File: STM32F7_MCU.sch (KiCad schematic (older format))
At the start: 49 parts, among them IC4 STM32F769IIT6, IC5 LD1117ADT33TR, Y1 25MHz, Y2 XTAL016178-85SMX

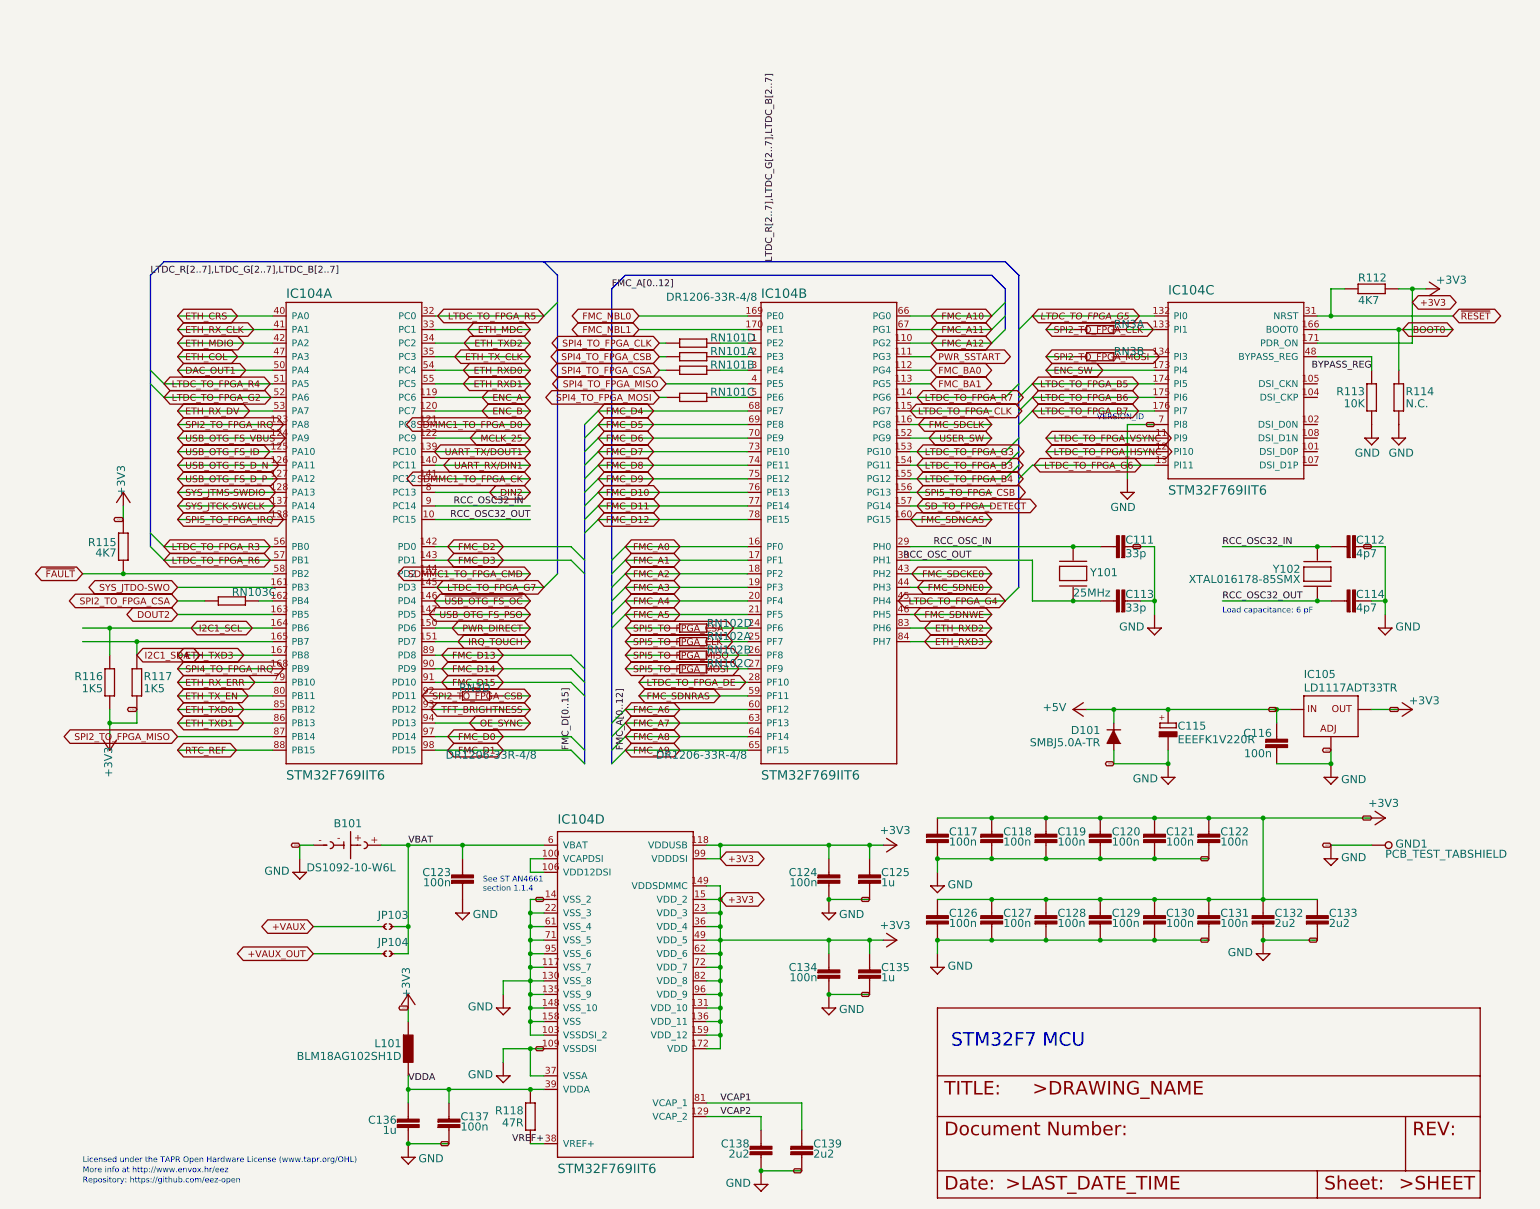
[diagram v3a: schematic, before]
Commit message: Removing BUS from STM32 - cleanup direct connections
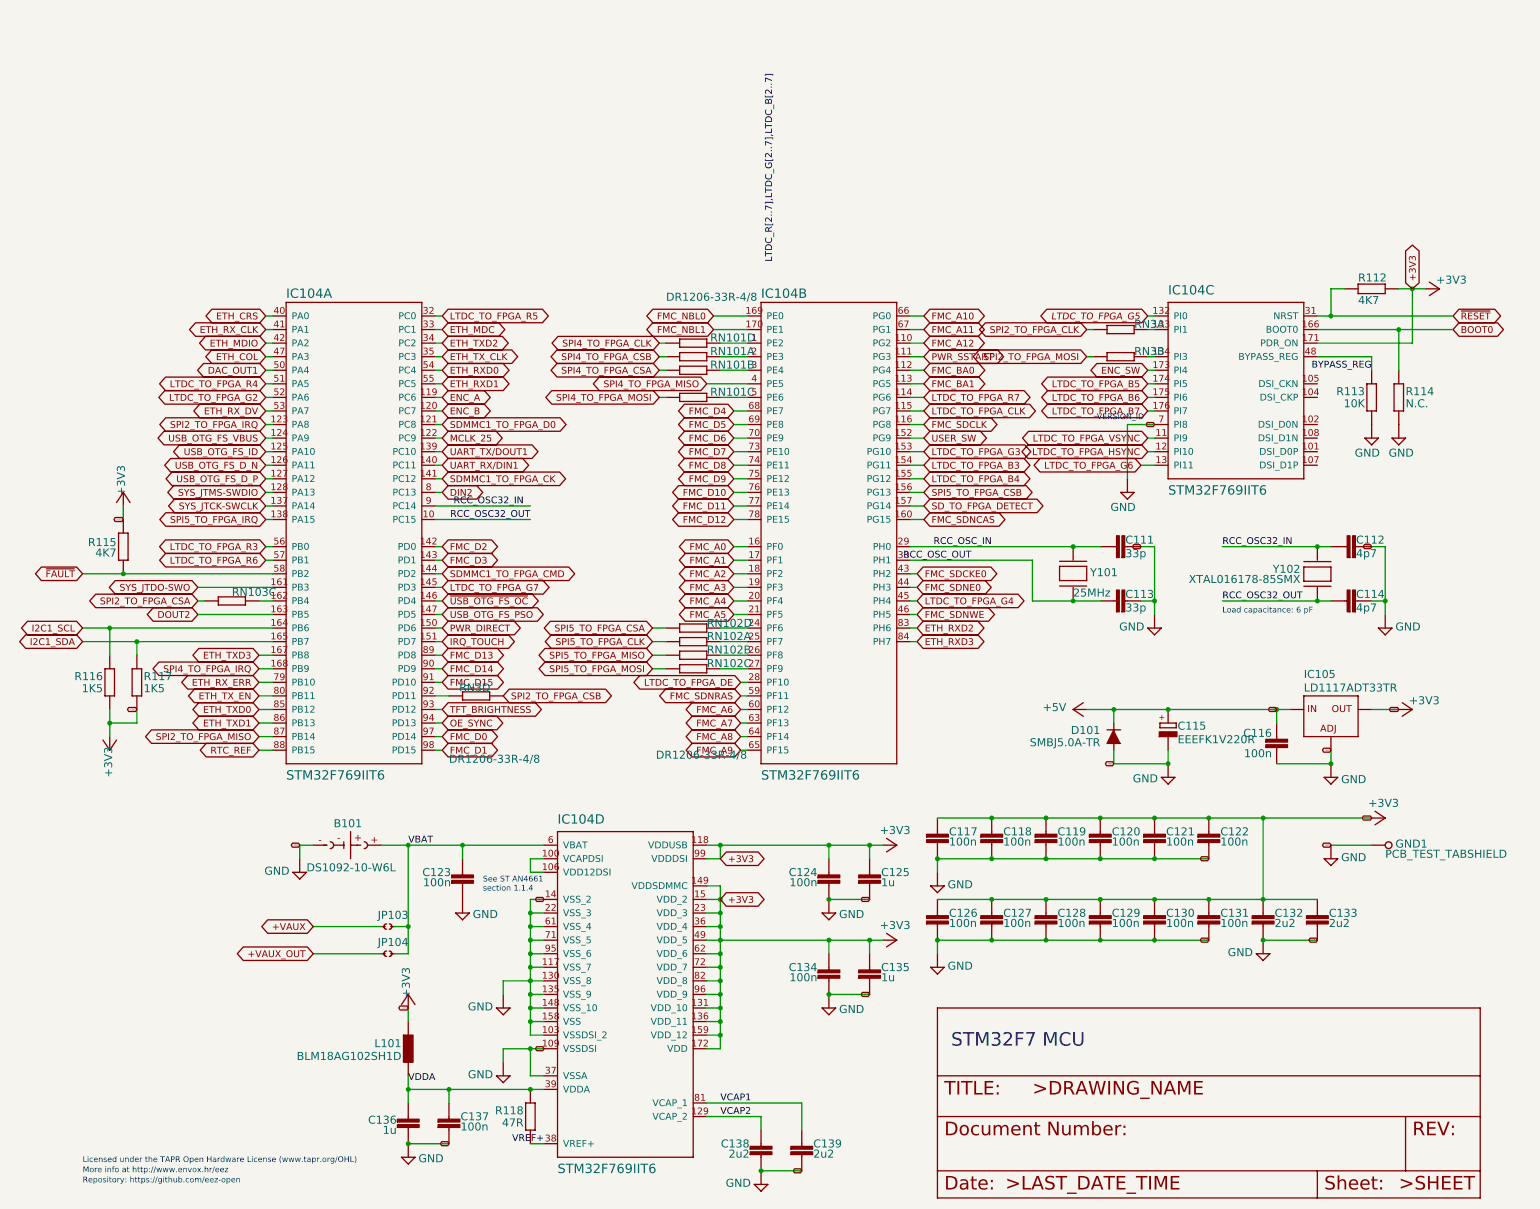
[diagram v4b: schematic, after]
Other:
- moved on the sheet: RN3A, RN3B

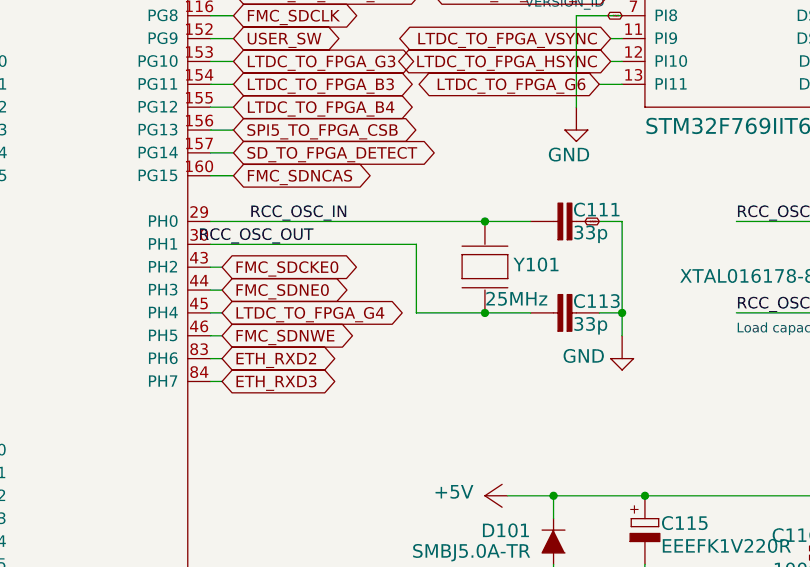
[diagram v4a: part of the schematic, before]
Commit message: Adding SPI from FPGA
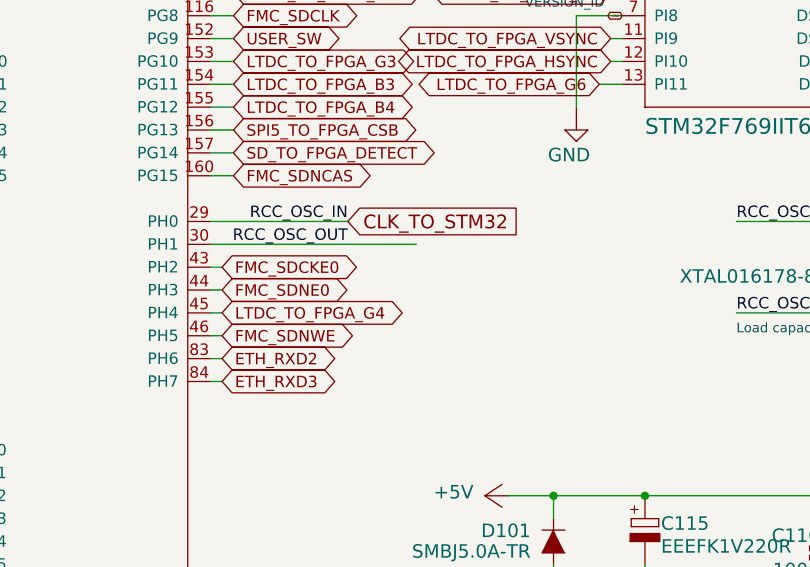
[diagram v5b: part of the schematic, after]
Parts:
- removed C11, C13: 33p, Capacitor_SMD:C_0603_1608Metric, symbol STM32F7_MCU-rescue:C-EUC0603-EEZ_DIB_MCU_r3B4-eagle-import
- removed Y1: 25MHz, EEZ DIB MCU r3B4:HC-49_4H, symbol STM32F7_MCU-rescue:XTALSMD-EEZ_DIB_MCU_r3B4-eagle-import
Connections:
- net RCC_OSC_IN renamed CLK_TO_STM32
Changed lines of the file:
@@
 Text GLabel 7200 4100 2    50   BiDi ~ 0
 FMC_SDNCAS
-Wire Wire Line
-	7100 4300 8300 4300
-Wire Wire Line
-	8500 4300 8300 4300
 Text Label 7700 4300 2    50   ~ 0
 RCC_OSC_IN
-Connection ~ 8300 4300
 Wire Wire Line
 	7100 4400 8000 4400
-Wire Wire Line
-	8000 4400 8000 4700
-Wire Wire Line
-	8000 4700 8300 4700
-Wire Wire Line
-	8500 4700 8300 4700
-Text Label 7550 4400 2    50   ~ 0
+Text Label 7700 4400 2    50   ~ 0
 RCC_OSC_OUT
-Connection ~ 8300 4700
 Text GLabel 7150 4500 2    50   BiDi ~ 0
 FMC_SDCKE0
@@
 GND
 Wire Wire Line
-	8800 4300 8900 4300
-Wire Wire Line
-	8900 4300 8900 4700
-Wire Wire Line
-	8900 4700 8900 4800
-Wire Wire Line
-	8800 4700 8900 4700
-Connection ~ 8900 4700
-Text GLabel 8800 4300 0    10   BiDi ~ 0
-GND
-Wire Wire Line
 	3700 8700 3400 8700
 Connection ~ 3400 8700
@@
 $EndComp
 $Comp
-L STM32F7_MCU-rescue:XTALSMD-EEZ_DIB_MCU_r3B4-eagle-import Y1
-U 1 1 BB35BB16
-P 8300 4500
-AR Path="/84DDC79DBB35BB16" Ref="Y1"  Part="1"
-AR Path="/5F88D05D/84DDC79DBB35BB16" Ref="Y1"  Part="1"
-AR Path="/5F88BD9A/84DDC79DBB35BB16" Ref="Y101"  Part="1"
-AR Path="/5F88BD9A/BB35BB16" Ref="Y101"  Part="1"
-F 0 "Y101" V 8275 4375 59  0000 R TNN
-F 1 "25MHz" V 8125 4500 59  0000 R TNN
-F 2 "EEZ DIB MCU r3B4:HC-49_4H" H 8300 4500 50  0001 C CNN
-F 3 "" H 8300 4500 50  0001 C CNN
-	1    8300 4500
-	0    -1   -1   0
-$EndComp
-$Comp
 L STM32F7_MCU-rescue:STM32F769IXT-EEZ_DIB_MCU_r3B4-eagle-import IC4
 U 1 1 B1CDB4F7
@@
 $EndComp
 $Comp
-L STM32F7_MCU-rescue:C-EUC0603-EEZ_DIB_MCU_r3B4-eagle-import C11
-U 1 1 B3BB1690
-P 8700 4300
-AR Path="/1EE302F0B3BB1690" Ref="C11"  Part="1"
-AR Path="/5F88D05D/1EE302F0B3BB1690" Ref="C11"  Part="1"
-AR Path="/5F88BD9A/1EE302F0B3BB1690" Ref="C111"  Part="1"
-AR Path="/5F88BD9A/B3BB1690" Ref="C111"  Part="1"
-F 0 "C111" V 8715 4285 59  0000 L TNN
-F 1 "33p" V 8615 4285 59  0000 L TNN
-F 2 "Capacitor_SMD:C_0603_1608Metric" H 8700 4300 50  0001 C CNN
-F 3 "" H 8700 4300 50  0001 C CNN
-	1    8700 4300
-	0    1    -1   0
-$EndComp
-$Comp
-L STM32F7_MCU-rescue:C-EUC0603-EEZ_DIB_MCU_r3B4-eagle-import C13
-U 1 1 7026A3DA
-P 8700 4700
-AR Path="/752FD70E7026A3DA" Ref="C13"  Part="1"
-AR Path="/5F88D05D/752FD70E7026A3DA" Ref="C13"  Part="1"
-AR Path="/5F88BD9A/752FD70E7026A3DA" Ref="C113"  Part="1"
-AR Path="/5F88BD9A/7026A3DA" Ref="C113"  Part="1"
-F 0 "C113" V 8715 4685 59  0000 L TNN
-F 1 "33p" V 8615 4685 59  0000 L TNN
-F 2 "Capacitor_SMD:C_0603_1608Metric" H 8700 4700 50  0001 C CNN
-F 3 "" H 8700 4700 50  0001 C CNN
-	1    8700 4700
-	0    1    -1   0
-$EndComp
-$Comp
 L STM32F7_MCU-rescue:GND-EEZ_DIB_MCU_r3B4-eagle-import #SUPPLY29
 U 1 1 0331A01D
@@
 F 3 "" H 4100 7700 50  0001 C CNN
 	1    4100 7700
-	-1   0    0    -1
-$EndComp
-$Comp
-L STM32F7_MCU-rescue:GND-EEZ_DIB_MCU_r3B4-eagle-import #SUPPLY19
-U 1 1 4114ABC6
-P 8900 4900
-AR Path="/D41E167D4114ABC6" Ref="#SUPPLY19"  Part="1"
-AR Path="/5F88D05D/D41E167D4114ABC6" Ref="#SUPPLY019"  Part="1"
-AR Path="/5F88BD9A/D41E167D4114ABC6" Ref="#SUPPLY019"  Part="1"
-AR Path="/5F88BD9A/4114ABC6" Ref="#SUPPLY019"  Part="1"
-F 0 "#SUPPLY019" H 8900 4900 50  0001 C CNN
-F 1 "GND" H 8975 4875 59  0000 L BNN
-F 2 "" H 8900 4900 50  0001 C CNN
-F 3 "" H 8900 4900 50  0001 C CNN
-	1    8900 4900
 	-1   0    0    -1
 $EndComp
@@
 Wire Wire Line
 	7100 3600 7200 3600
+Text GLabel 7700 4300 2    60   Input ~ 0
+CLK_TO_STM32
+Wire Wire Line
+	7100 4300 7700 4300
 $EndSCHEMATC

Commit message: Adding DIB_V2 connector for SERDES, change battery, initial power fixes power
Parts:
- B1: footprint EEZ DIB MCU r3B4:DS1092-10-W6L -> Battery:Battery_Panasonic_CR1025-VSK_Vertical_CircularHoles
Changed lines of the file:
@@
 EESchema Schematic File Version 4
-EELAYER 30 0
+LIBS:ulx3s-cache
+EELAYER 29 0
 EELAYER END
 $Descr User 12325 9925
@@
 F 0 "B101" H 2850 6625 59  0000 L BNN
 F 1 "DS1092-10-W6L" H 2650 6300 59  0000 L BNN
-F 2 "EEZ DIB MCU r3B4:DS1092-10-W6L" H 2900 6500 50  0001 C CNN
+F 2 "Battery:Battery_Panasonic_CR1025-VSK_Vertical_CircularHoles" H 2900 6500 50  0001 C CNN
 F 3 "" H 2900 6500 50  0001 C CNN
 	1    2900 6500
